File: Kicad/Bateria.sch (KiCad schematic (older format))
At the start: 2 parts, among them P2 CONN_01X02, SW1 SW_PUSH

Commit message: Cambios en tamaño de pinheaders
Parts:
- P2, SW1: footprint EMG:Pin_Header_Straight_1x02_Pitch2.54mm -> EMG:Pin_Header_Straight_1x02_Pitch1.27mm
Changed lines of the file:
@@
 F 0 "SW1" H 4850 3760 50  0000 C CNN
 F 1 "SW_PUSH" H 4700 3570 50  0000 C CNN
-F 2 "EMG:Pin_Header_Straight_1x02_Pitch2.54mm" H 4700 3650 50  0001 C CNN
+F 2 "EMG:Pin_Header_Straight_1x02_Pitch1.27mm" H 4700 3650 50  0001 C CNN
 F 3 "" H 4700 3650 50  0000 C CNN
 	1    4700 3650
@@
 F 0 "P2" H 5250 3600 50  0000 C CNN
 F 1 "CONN_01X02" V 5350 3450 50  0000 C CNN
-F 2 "EMG:Pin_Header_Straight_1x02_Pitch2.54mm" H 5250 3450 50  0001 C CNN
+F 2 "EMG:Pin_Header_Straight_1x02_Pitch1.27mm" H 5250 3450 50  0001 C CNN
 F 3 "" H 5250 3450 50  0000 C CNN
 	1    5250 3450

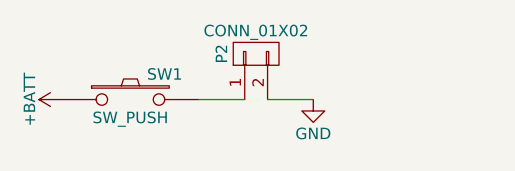
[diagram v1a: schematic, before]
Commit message: Cambiado el switch por uno de punto medio. Aumento de ancho en pistas de alimentación. Plano de masa
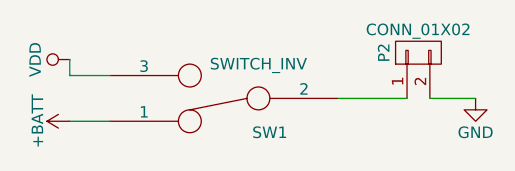
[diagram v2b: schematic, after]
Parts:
- removed SW1: SW_PUSH, EMG:Pin_Header_Straight_1x02_Pitch1.27mm, symbol SW_PUSH
- added SW1: SWITCH_INV, EMG:Pin_Header_Straight_1x03_Pitch1.27mm, symbol SWITCH_INV
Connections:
- net +BATT: now also SW1.1
- net at P2.1 (P1): now also SW1.2
- new net VDD: SW1.3
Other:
- moved on the sheet: P2
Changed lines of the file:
@@
 L +BATT #PWR021
 U 1 1 57DDA8D2
-P 4400 3650
-F 0 "#PWR021" H 4400 3500 50  0001 C CNN
-F 1 "+BATT" H 4400 3790 50  0000 C CNN
-F 2 "" H 4400 3650 50  0000 C CNN
-F 3 "" H 4400 3650 50  0000 C CNN
-	1    4400 3650
+P 4435 3745
+F 0 "#PWR021" H 4435 3595 50  0001 C CNN
+F 1 "+BATT" H 4435 3885 50  0000 C CNN
+F 2 "" H 4435 3745 50  0000 C CNN
+F 3 "" H 4435 3745 50  0000 C CNN
+	1    4435 3745
 	0    -1   -1   0
 $EndComp
@@
 L GND #PWR022
 U 1 1 57FAD2FA
-P 5500 3650
-F 0 "#PWR022" H 5500 3400 50  0001 C CNN
-F 1 "GND" H 5500 3500 50  0000 C CNN
-F 2 "" H 5500 3650 50  0000 C CNN
-F 3 "" H 5500 3650 50  0000 C CNN
-	1    5500 3650
-	1    0    0    -1
-$EndComp
-$Comp
-L SW_PUSH SW1
-U 1 1 583EE592
-P 4700 3650
-F 0 "SW1" H 4850 3760 50  0000 C CNN
-F 1 "SW_PUSH" H 4700 3570 50  0000 C CNN
-F 2 "EMG:Pin_Header_Straight_1x02_Pitch1.27mm" H 4700 3650 50  0001 C CNN
-F 3 "" H 4700 3650 50  0000 C CNN
-	1    4700 3650
+P 6210 3645
+F 0 "#PWR022" H 6210 3395 50  0001 C CNN
+F 1 "GND" H 6210 3495 50  0000 C CNN
+F 2 "" H 6210 3645 50  0000 C CNN
+F 3 "" H 6210 3645 50  0000 C CNN
+	1    6210 3645
 	1    0    0    -1
 $EndComp
@@
 L CONN_01X02 P2
 U 1 1 58BC865C
-P 5250 3450
-F 0 "P2" H 5250 3600 50  0000 C CNN
-F 1 "CONN_01X02" V 5350 3450 50  0000 C CNN
-F 2 "EMG:Pin_Header_Straight_1x02_Pitch1.27mm" H 5250 3450 50  0001 C CNN
-F 3 "" H 5250 3450 50  0000 C CNN
-	1    5250 3450
+P 5960 3445
+F 0 "P2" H 5960 3595 50  0000 C CNN
+F 1 "CONN_01X02" V 6060 3445 50  0000 C CNN
+F 2 "EMG:Pin_Header_Straight_1x02_Pitch1.27mm" H 5960 3445 50  0001 C CNN
+F 3 "" H 5960 3445 50  0000 C CNN
+	1    5960 3445
 	0    -1   -1   0
 $EndComp
 Wire Wire Line
-	5500 3650 5300 3650
+	6210 3645 6010 3645
 Wire Wire Line
-	5000 3650 5200 3650
+	5610 3645 5910 3645
+$Comp
+L SWITCH_INV SW1
+U 1 1 58DE8350
+P 5110 3645
+F 0 "SW1" H 4910 3795 50  0000 C CNN
+F 1 "SWITCH_INV" H 4960 3495 50  0000 C CNN
+F 2 "EMG:Pin_Header_Straight_1x03_Pitch1.27mm" H 5110 3645 50  0001 C CNN
+F 3 "" H 5110 3645 50  0000 C CNN
+	1    5110 3645
+	-1   0    0    1
+$EndComp
+Wire Wire Line
+	4435 3745 4610 3745
+$Comp
+L VDD #PWR023
+U 1 1 58DE850D
+P 4435 3475
+F 0 "#PWR023" H 4435 3325 50  0001 C CNN
+F 1 "VDD" H 4435 3625 50  0000 C CNN
+F 2 "" H 4435 3475 50  0000 C CNN
+F 3 "" H 4435 3475 50  0000 C CNN
+	1    4435 3475
+	0    -1   -1   0
+$EndComp
+Wire Wire Line
+	4610 3545 4435 3545
+Wire Wire Line
+	4435 3545 4435 3475
 $EndSCHEMATC
